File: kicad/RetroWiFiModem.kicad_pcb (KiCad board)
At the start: 2 copper layers, 102.5 x 66.1 mm, 38 parts, among them CON1 5V centre +, P1 RS232, U1 74HCT245, U2 MAX3232, U3 74HC32, U4 3.3V reg, U5 WeMos_mini_D1

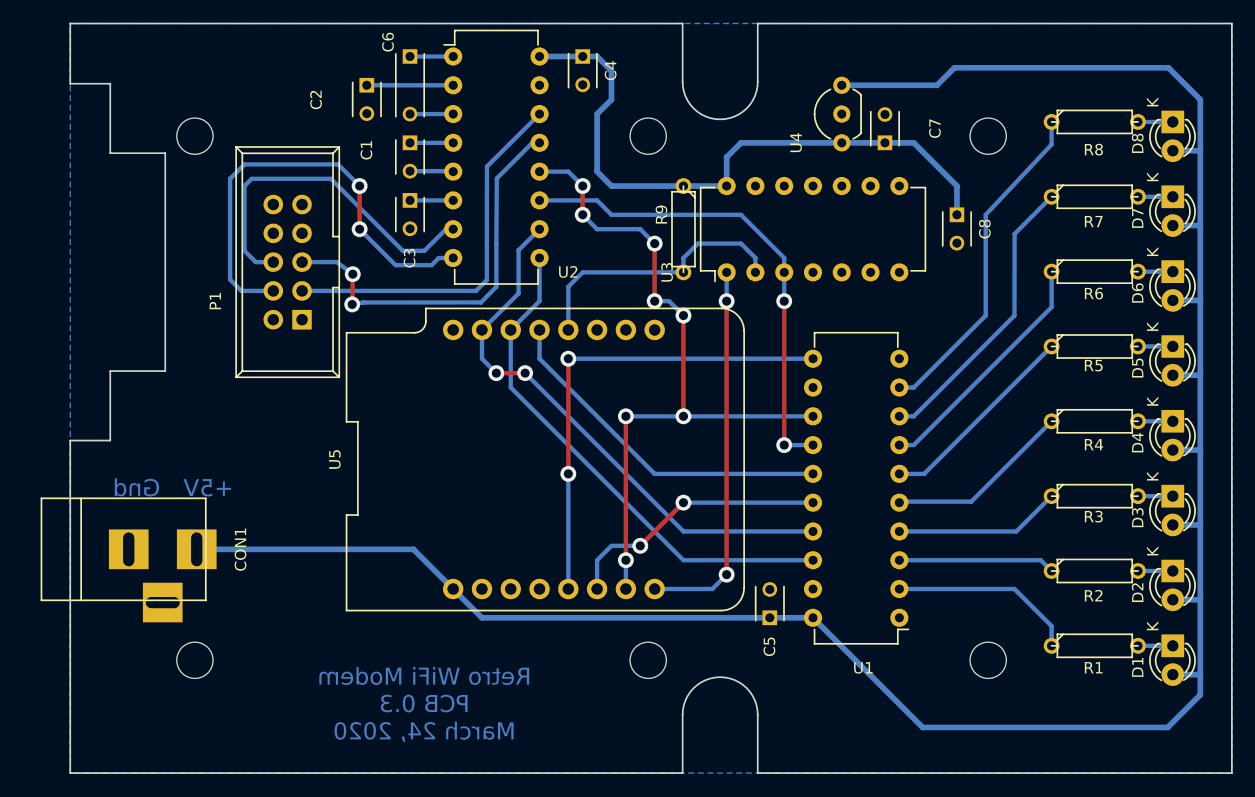
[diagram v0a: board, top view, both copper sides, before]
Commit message: update symbols and footprints for KiCad 5.1.2
* remaps all symbols and footprints to those present in KiCad 5.1.2.
* add mounting holes to schematics
* PCB has been touched up due to footprint changes, but should remain
  almost identical to the original
* NOTE: schematic now has some warnings about tristate<->output connections

symbols and footprints are mapped as follows:

Designator	Old symbol	Old package	New symbol	New package
C1,C2,C3,C4,C5,C8	C_Small	Capacitors_THT:C_Disc_D3_P2.5	Device:C_Small	Capacitor_THT:C_Disc_D3.0mm_W2.0mm_P2.50mm
C6	C_Small	Capacitors_THT:C_Disc_D3_P5	Device:C_Small	Capacitor_THT:C_Disc_D3.0mm_W2.0mm_P2.50mm
C7	C_Small	Capacitors_THT:C_Disc_D3_P2.5	Device:C_Small	Capacitor_THT:C_Disc_D3.0mm_W2.0mm_P2.50mm
CON1	BARREL_JACK	Connectors:BARREL_JACK	Connector:Barrel_Jack_Switch	Connector_BarrelJack:BarrelJack_Horizontal
D1,D2,D3,D4,D5,D6,D7,D8	LED	LEDs:LED-3MM	Device:LED	LED_THT:LED_D3.0mm
P1	CONN_02X05	Connectors:IDC_Header_Straight_10pins	Conn_02x05_Odd_Even	Connector_IDC:IDC-Header_2x05_P2.54mm_Vertical
U2	MAX232	Housings_DIP:DIP-16_W7.62mm	Interface_UART:MAX232	Package_DIP:DIP-16_W7.62mm
U3	74LS32	Housings_DIP:DIP-14_W7.62mm	74xx:74LS32	Package_DIP:DIP-14_W7.62mm
U4	LM2931AZ-3.3/5.0	TO_SOT_Packages_THT:TO-92_Inline_Wide	Regulator_Linear:LP2950-3.3_TO92	Package_TO_SOT_THT:TO-92L_Inline_Wide
U5	WeMos_mini	WEMOS_D1_Mini:wemos-d1-mini-with-pin-header-and-connector	RetroWiFiModem:WeMos_mini	footprint:wemos-d1-mini
U1	74ACT245	Housings_DIP:DIP-20_W7.62mm	74xx:74HC245	Package_DIP:DIP-20_W7.62mm
R1,R2,R3,R4,R5,R6,R7,R8	R_US	Discret:R3	Device:R	Resistor_THT:R_Axial_DIN0204_L3.6mm_D1.6mm_P7.62mm_Horizontal
R9	R_US	Discret:R3	Device:R	Resistor_THT:R_Axial_DIN0204_L3.6mm_D1.6mm_P7.62mm_Horizontal
H1,H2,H3,H4,H5,H6		Mounting_Holes:MountingHole_3.2mm_Hammond_1593	Mechanical:MountingHole	MountingHole:MountingHole_3.2mm_M3
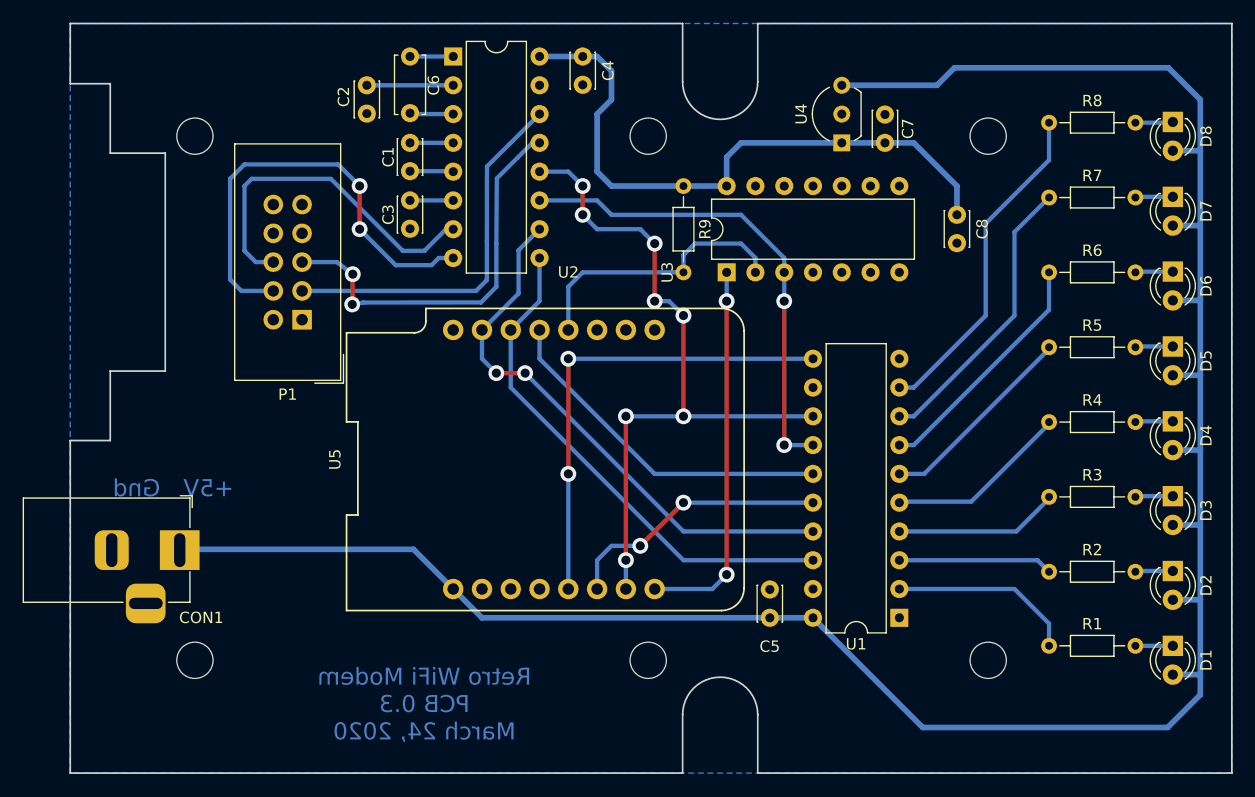
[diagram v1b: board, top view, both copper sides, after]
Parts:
- removed ? (x6): , Mounting_Holes:MountingHole_3.2mm_Hammond_1593
- added H1: MountingHole, MountingHole:MountingHole_3.2mm_M3, F.Cu at (119.5, 85.8)
- added H2: MountingHole, MountingHole:MountingHole_3.2mm_M3, F.Cu at (119.5, 132.0)
- added H3: MountingHole, MountingHole:MountingHole_3.2mm_M3, F.Cu at (159.4, 85.8)
- added H4: MountingHole, MountingHole:MountingHole_3.2mm_M3, F.Cu at (159.4, 132.0)
- added H5: MountingHole, MountingHole:MountingHole_3.2mm_M3, F.Cu at (189.4, 85.8)
- added H6: MountingHole, MountingHole:MountingHole_3.2mm_M3, F.Cu at (189.4, 132.0)
- C1, C2, C3, C4, C5, C7, C8: footprint Capacitors_THT:C_Disc_D3_P2.5 -> Capacitor_THT:C_Disc_D3.0mm_W2.0mm_P2.50mm
- C6: footprint Capacitors_THT:C_Disc_D3_P5 -> Capacitor_THT:C_Disc_D5.0mm_W2.5mm_P5.00mm
- CON1: value 5V centre + -> BARREL_JACK; footprint Connectors:BARREL_JACK -> Connector_BarrelJack:BarrelJack_Horizontal
- D1: value RTS -> TLPR5600; footprint LEDs:LED-3MM -> LED_THT:LED_D3.0mm
- D2: value CTS -> TLPR5600; footprint LEDs:LED-3MM -> LED_THT:LED_D3.0mm
- D3: value DCD -> TLPR5600; footprint LEDs:LED-3MM -> LED_THT:LED_D3.0mm
- D4: value RI -> TLPR5600; footprint LEDs:LED-3MM -> LED_THT:LED_D3.0mm
- D5: value RxD -> TLPR5600; footprint LEDs:LED-3MM -> LED_THT:LED_D3.0mm
- D6: value TxD -> TLPR5600; footprint LEDs:LED-3MM -> LED_THT:LED_D3.0mm
- D7: value DTR -> TLPR5600; footprint LEDs:LED-3MM -> LED_THT:LED_D3.0mm
- D8: value DSR -> TLPR5600; footprint LEDs:LED-3MM -> LED_THT:LED_D3.0mm
- P1: value RS232 -> CONN_02X05; footprint Connectors:IDC_Header_Straight_10pins -> Connector_IDC:IDC-Header_2x05_P2.54mm_Vertical
- R1, R2, R3, R4, R5, R6, R7, R8: value 560 -> 560R; footprint Discret:R3 -> Resistor_THT:R_Axial_DIN0204_L3.6mm_D1.6mm_P7.62mm_Horizontal
- R9: footprint Discret:R3 -> Resistor_THT:R_Axial_DIN0204_L3.6mm_D1.6mm_P7.62mm_Horizontal
- U1: value 74HCT245 -> 74HC245; footprint Housings_DIP:DIP-20_W7.62mm -> Package_DIP:DIP-20_W7.62mm
- U2: footprint Housings_DIP:DIP-16_W7.62mm -> Package_DIP:DIP-16_W7.62mm
- U3: footprint Housings_DIP:DIP-14_W7.62mm -> Package_DIP:DIP-14_W7.62mm
- U4: value 3.3V reg -> LP2950ACZ-3.3; footprint TO_SOT_Packages_THT:TO-92_Inline_Wide -> Package_TO_SOT_THT:TO-92L_Inline_Wide
- U5: value WeMos_mini_D1 -> WeMos_D1_mini; footprint WEMOS_D1_Mini:wemos-d1-mini-with-pin-header-and-connector -> RetroWiFiModem-footprints:wemos-d1-mini
- moved CON1 4.70 mm to (118.1, 122.3)
- moved R2 4.04 mm to (194.8, 124.2)
- moved R3 4.04 mm to (194.8, 117.6)
- moved R4 4.04 mm to (194.8, 111.0)
- moved R5 4.04 mm to (194.8, 104.4)
- moved R6 4.04 mm to (194.8, 97.8)
- moved R7 4.04 mm to (194.8, 91.2)
- moved R8 4.04 mm to (194.8, 84.6)
- moved R1 4.04 mm to (194.8, 130.7)
- moved R9 3.81 mm to (162.6, 90.2)
- moved C6 2.54 mm to (138.4, 78.7)
- turned P1 to 180 degrees
